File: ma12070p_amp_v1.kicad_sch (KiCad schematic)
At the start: 83 parts, among them U1 MAX16956AUBD/V+, U2 MA12070P

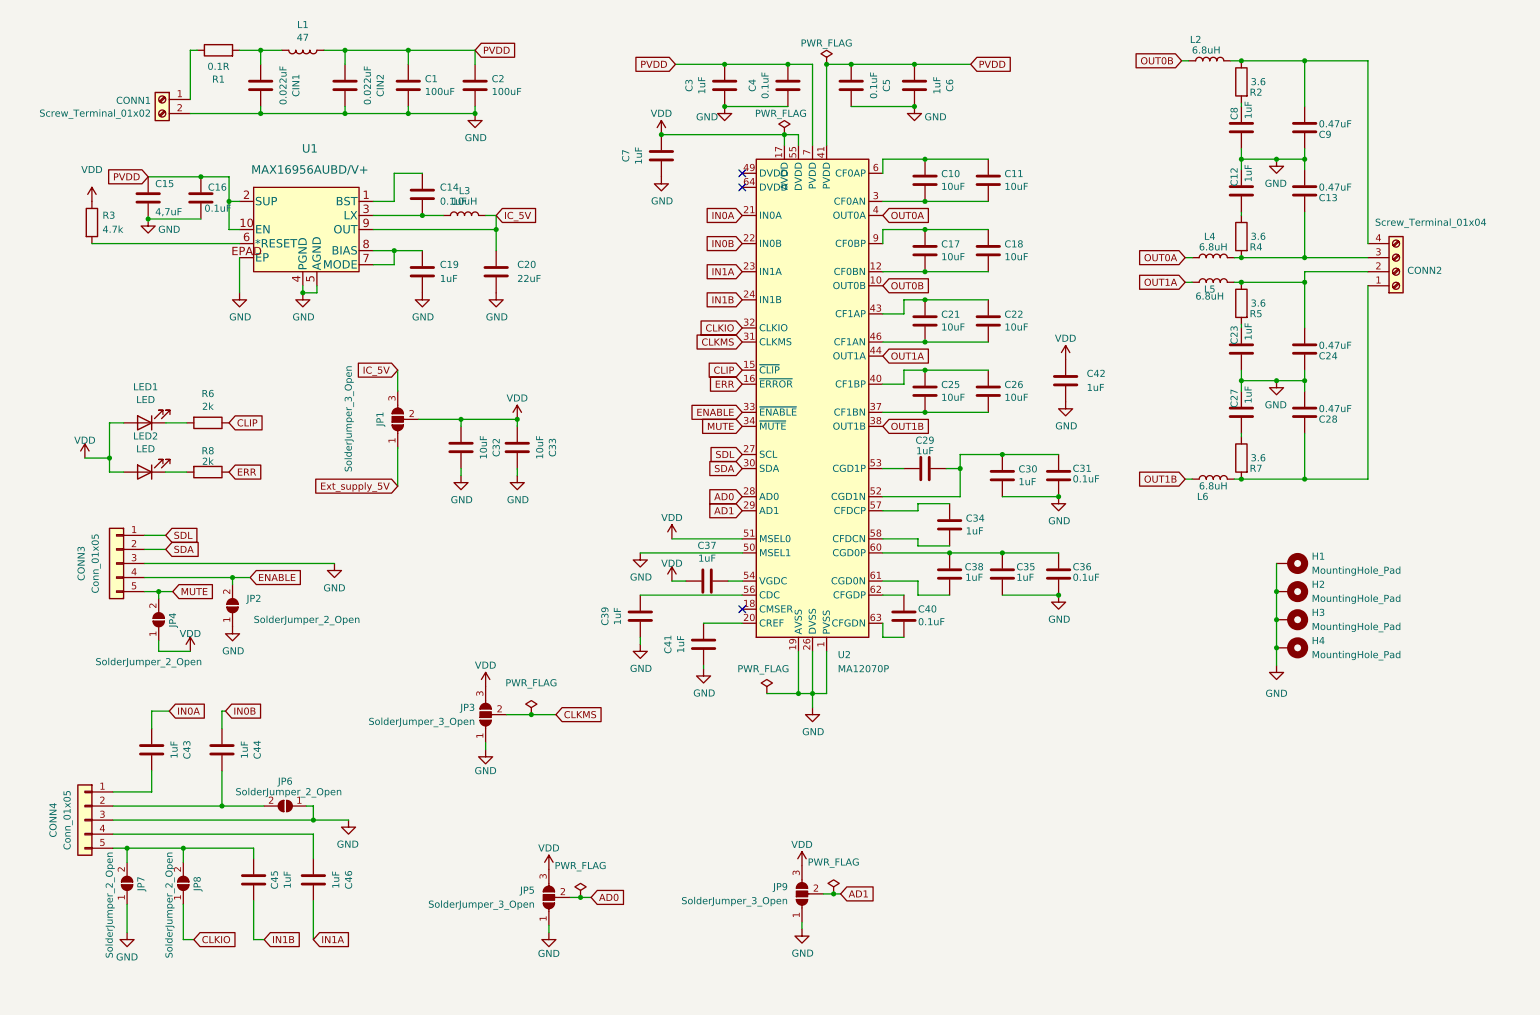
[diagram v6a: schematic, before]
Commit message: layout change of power supp
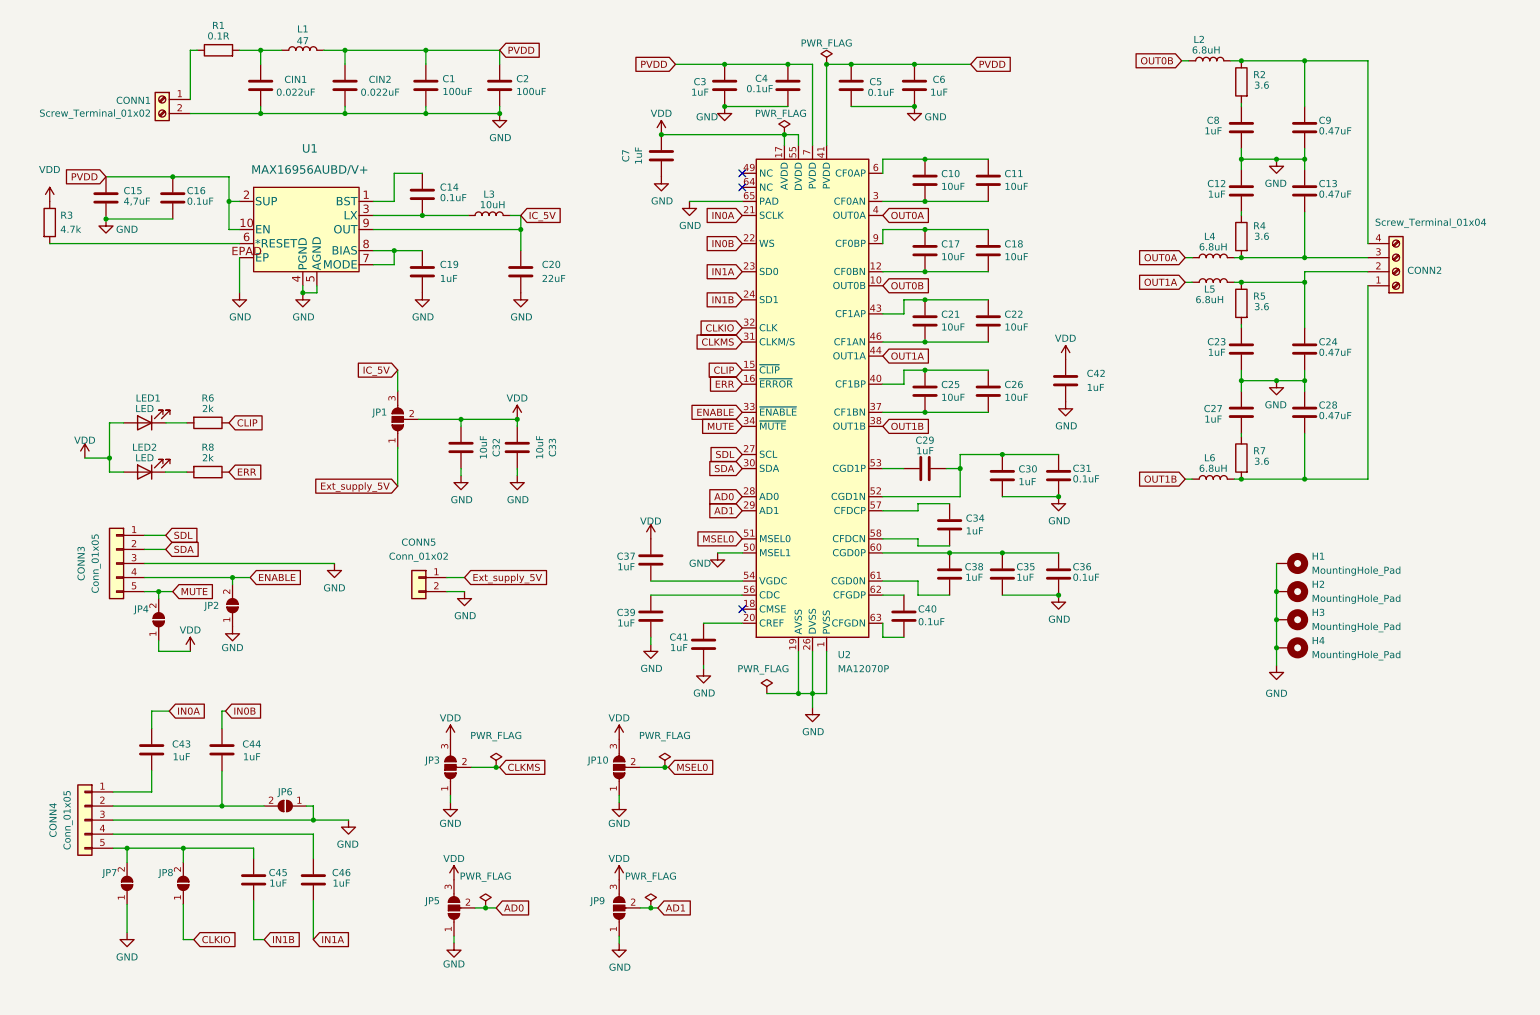
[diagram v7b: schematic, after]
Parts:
- added CONN5: Conn_01x02, Connector_PinHeader_2.54mm:PinHeader_1x02_P2.54mm_Vertical, symbol Connector_Generic:Conn_01x02
- added JP10: SolderJumper_3_Open, Jumper:SolderJumper-3_P1.3mm_Open_Pad1.0x1.5mm, symbol Jumper:SolderJumper_3_Open
- U2: symbol Amplifier_Audio:MA12070P -> ma12070p_v1:MA12070P
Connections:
- net Ext_supply_5V: now also CONN5.1 (Pin_1)
- net GND: now also U2.65 (PAD), CONN5.2 (Pin_2), JP10.1 (A)
- net PVDD: now also L1.2; no longer L1.1
- net VDD: now also C37.1, JP10.3 (B); no longer C37.2, U2.51 (MSEL0)
- net at U2.54 (VGDC): now also C37.2; no longer C37.1
- net at CIN1.2, R1.2: now also L1.1; no longer L1.2
- new net MSEL0: JP10.2 (C), U2.51 (MSEL0)
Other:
- moved on the sheet: C1, C15, C16, C2, C20, C37, C39, JP3, JP5, JP9, L1, L3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
